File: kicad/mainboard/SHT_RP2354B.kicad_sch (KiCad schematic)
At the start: 61 parts, among them J3 USB_B_Micro, J7 Conn_01x03_Shielded, J8 Conn_01x04_Shielded, Q1 AO3401A, SW2 SW_Push_RUN, SW4 SW_Push_BOOT, U2 MCP73831-2-OT, U3 RP2350_80QFN, U5 TPS63031DSK, U6 MAINSW_CUS-12TB, U7 TFTSW_CUS-12TB, Y1 X322512MSB4SI

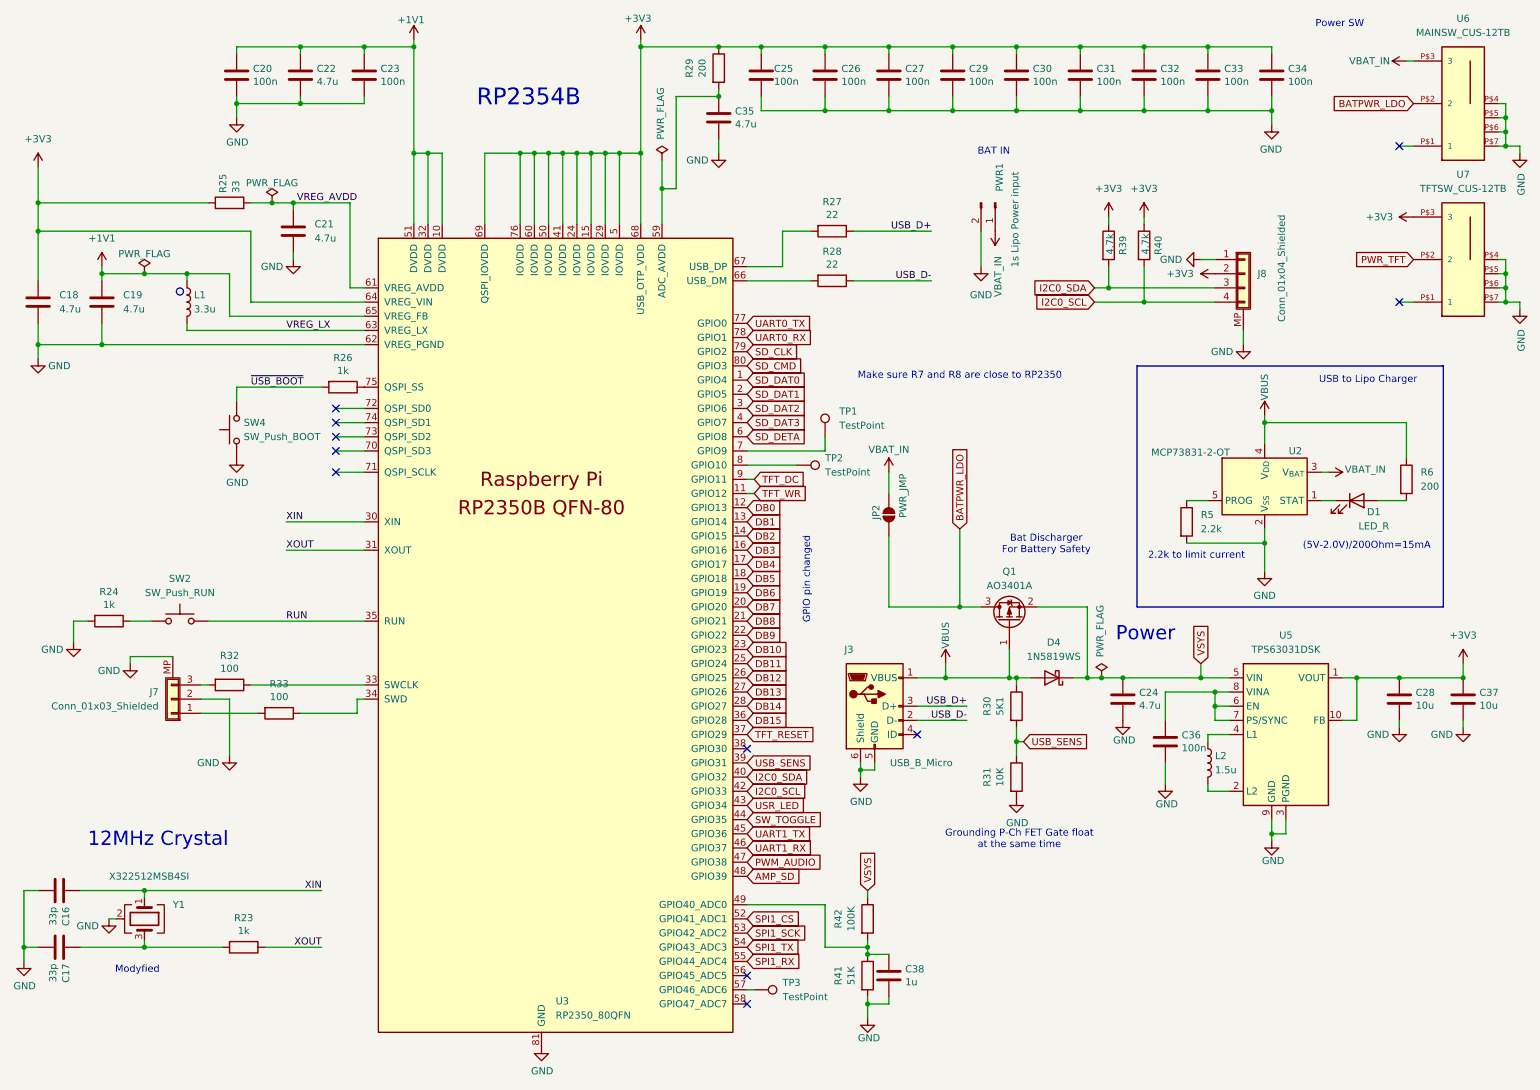
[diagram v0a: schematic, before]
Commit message: 0.960 ソフトウェア＋ドキュメント KiCad v7 基板
普段編集しないモジュールを src/ へ移動し、README を v7 に更新

■ src/ への移動（Arduino IDE のタブ削減）
Arduino IDE はスケッチ直下のファイルを全部タブに出すため 28 個まで増え、
目的のファイルを探しづらくなっていた。仕様が固まっていて普段いじらない
4 モジュールを src/ へ移し、タブを 20 個に減らした。

  src/button.*     ボタン入力・メニュー
  src/sound.*      音声出力（WAV・トーン）
  src/vectormap.*  ベクタ地図の描画
  src/imulog.*     生 IMU ロガー

src/ 配下もコンパイルされるが IDE のタブには出ない。裏を返すと IDE からは
編集できなくなるので、これらは VSCode 等で編集すること。
またスケッチ直下は include パスに入っていないため、src/ の中からルート側の
ヘッダを参照するときは "../mysd.h" のように 1 段戻る必要がある。
この経緯と注意点は GPS_TFT_map.ino のヘッダに残した。

#include は 27 箇所を書き換え、全 104 件が実在するパスへ解決することを確認。

■ 併せて修正
button.cpp の #include "Button.h" が大文字始まりだった。macOS は
ファイルシステムが大文字小文字を区別しないため通っていたが、Linux では
壊れる。"button.h" に修正。

■ README を v7 に更新
 * タイトルとスペックを v7 へ。ソフトウェアバージョン 0.942 → 0.960
 * PONS Link（機体⇄ボート テレメトリ無線）の節を新設。3 台構成、下り一方向に
   した理由、無線パラメータ、実測 350m。設計の詳細は docs/pons_link.md へ
 * BNO085 を β 試験版から標準搭載へ。SPI 接続にした理由も記載
 * マイコンを RP2350B（外付け FLASH 16MB）と明記
 * PCBA とは別に発注する部品の一覧表（Digikey / マルツ / 秋月）を追加
 * 警告音・SD ログ・使用部品に無線関連を追記

重量とバッテリー持続時間は v7 実機での計測待ちのため、v6 β版の参考値と
PONS Link の消費電流だけを記載した。水面での到達距離も未確認と明記。

普段編集しないモジュールを src/ へ移動し、README を v7 に更新

■ src/ への移動（Arduino IDE のタブ削減）
Arduino IDE はスケッチ直下のファイルを全部タブに出すため 28 個まで増え、
目的のファイルを探しづらくなっていた。仕様が固まっていて普段いじらない
4 モジュールを src/ へ移し、タブを 20 個に減らした。

  src/button.*     ボタン入力・メニュー
  src/sound.*      音声出力（WAV・トーン）
  src/vectormap.*  ベクタ地図の描画
  src/imulog.*     生 IMU ロガー

src/ 配下もコンパイルされるが IDE のタブには出ない。裏を返すと IDE からは
編集できなくなるので、これらは VSCode 等で編集すること。
またスケッチ直下は include パスに入っていないため、src/ の中からルート側の
ヘッダを参照するときは "../mysd.h" のように 1 段戻る必要がある。
この経緯と注意点は GPS_TFT_map.ino のヘッダに残した。

#include は 27 箇所を書き換え、全 104 件が実在するパスへ解決することを確認。

■ 併せて修正
button.cpp の #include "Button.h" が大文字始まりだった。macOS は
ファイルシステムが大文字小文字を区別しないため通っていたが、Linux では
壊れる。"button.h" に修正。

■ README を v7 に更新
 * タイトルとスペックを v7 へ。ソフトウェアバージョン 0.942 → 0.960
 * PONS Link（機体⇄ボート テレメトリ無線）の節を新設。3 台構成、下り一方向に
   した理由、無線パラメータ、実測 350m。設計の詳細は docs/pons_link.md へ
 * BNO085 を β 試験版から標準搭載へ。SPI 接続にした理由も記載
 * マイコンを RP2350B（外付け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
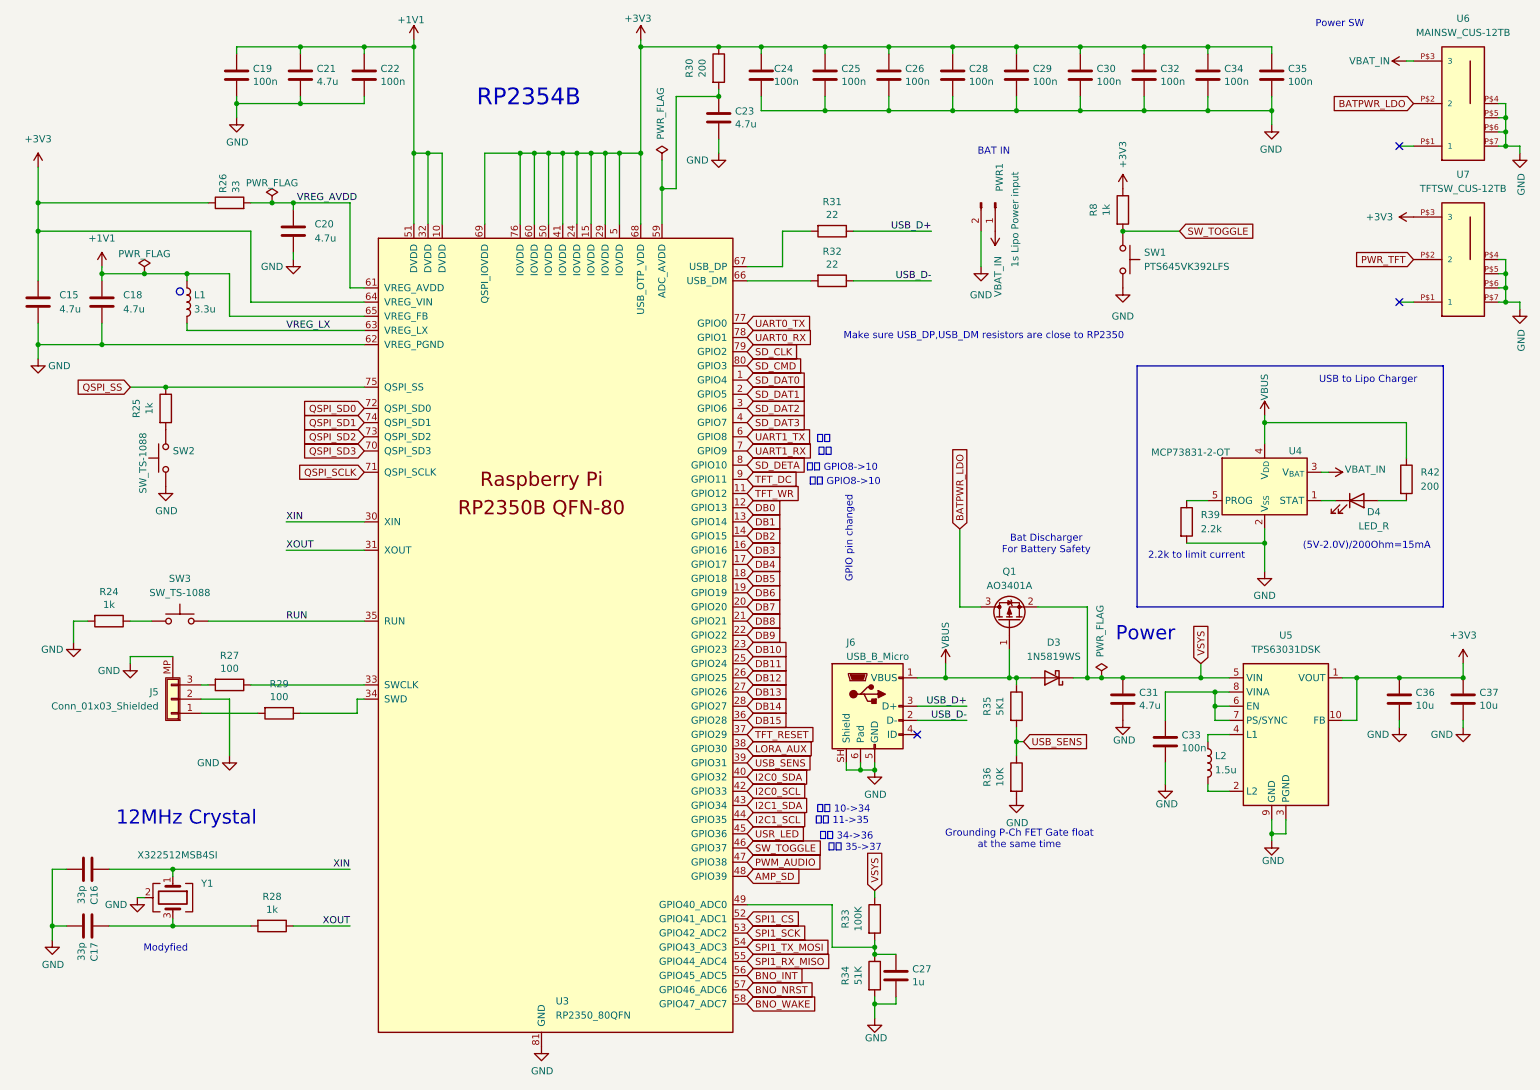
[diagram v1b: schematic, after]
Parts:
- removed J8: Conn_01x04_Shielded, Connector_JST:JST_SH_SM04B-SRSS-TB_1x04-1MP_P1.00mm_Horizontal, symbol Connector_Generic_Shielded:Conn_01x04_Shielded
- removed JP2: PWR_JMP, Jumper:SolderJumper-2_P1.3mm_Open_RoundedPad1.0x1.5mm, symbol Jumper:SolderJumper_2_Open
- removed R39, R40: 4.7k, Resistor_SMD:R_0402_1005Metric, symbol Device:R
- removed TP1, TP2, TP3: TestPoint, TestPoint:TestPoint_THTPad_D1.5mm_Drill0.7mm, symbol Connector:TestPoint
- added R8: 1k, Resistor_SMD:R_0402_1005Metric, symbol Device:R
- added SW1: PTS645VK392LFS, Button_Switch_THT:SW_Tactile_SPST_Angled_PTS645Vx39-2LFS, symbol Switch:SW_Push
- PWR1: LCSC C5251182 -> C173752; now in the parts list
- SW2: renamed from SW4; value SW_Push_BOOT -> SW_TS-1088; footprint Button_Switch_SMD:SW_Push_1P1T_NO_Vertical_Wuerth_434133025816 -> GPS_TFT:TS-1088-AR02016; LCSC C5504987 -> C720477; now in the parts list
- SW3: renamed from SW2; value SW_Push_RUN -> SW_TS-1088; footprint Button_Switch_SMD:SW_Push_1P1T_NO_Vertical_Wuerth_434133025816 -> GPS_TFT:TS-1088-AR02016; LCSC C5504987 -> C720477; now in the parts list
- U3: LCSC C39843328 -> C42415655
- U6, U7: footprint GPS_TFT:CUS-12B -> GPS_TFT:CUS-12TB
- renumbered C18 to C15, C19 to C18, C20 to C19, C21 to C20, C22 to C21, C23 to C22, C35 to C23, C25 to C24, C26 to C25, C27 to C26, C38 to C27, C29 to C28, C30 to C29, C31 to C30, C24 to C31, C36 to C33, C33 to C34, C34 to C35, C28 to C36, D4 to D3, D1 to D4, J7 to J5, J3 to J6, R26 to R25, R25 to R26, R32 to R27, R23 to R28, R33 to R29, R29 to R30, R27 to R31, R28 to R32, R42 to R33, R41 to R34, R30 to R35, R31 to R36, R5 to R39, R6 to R42, U2 to U4
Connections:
- net +3V3: now also R8.1
- net GND: now also J6.SH (Shield), SW1.2
- net SD_DETA: now also U3.8 (GPIO10); no longer U3.6 (GPIO8)
- net SW_TOGGLE: now also U3.46 (GPIO37), R8.2, SW1.1; no longer U3.44 (GPIO35)
- net UART1_RX: now also U3.7 (GPIO9); no longer U3.46 (GPIO37)
- net UART1_TX: now also U3.6 (GPIO8); no longer U3.45 (GPIO36)
- net USR_LED: now also U3.45 (GPIO36); no longer U3.43 (GPIO34)
- net BNO_NRST: now reaches U3.57 (GPIO46_ADC6)
- net LORA_AUX: now reaches U3.38 (GPIO30)
- net BNO_INT: now reaches U3.56 (GPIO45_ADC5)
- net BNO_WAKE: now reaches U3.58 (GPIO47_ADC7)
- net QSPI_SD3: now reaches U3.70 (QSPI_SD3)
- net QSPI_SCLK: now reaches U3.71 (QSPI_SCLK)
- net QSPI_SD0: now reaches U3.72 (QSPI_SD0)
- net QSPI_SD2: now reaches U3.73 (QSPI_SD2)
- net QSPI_SD1: now reaches U3.74 (QSPI_SD1)
- net QSPI_SS: now reaches R25.1, U3.75 (QSPI_SS)
- net SPI1_RX renamed SPI1_RX_MISO
- net SPI1_TX renamed SPI1_TX_MOSI
- net ~{USB_BOOT}: no longer names the net of R25.2, SW2.2
- new net I2C1_SCL: U3.44 (GPIO35)
- new net I2C1_SDA: U3.43 (GPIO34)
- no-connect marks 11 -> 3
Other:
- note added: "Make sure USB_DP,USB_DM resistors are close to RP2350"
- note added: "移動"
- note added: "移動 10->34"
- note added: "移動 11->35"
- note added: "移動 34->36"
- note added: "移動 35->37"
- note added: "移動 GPIO8->10"
- note removed: "Make sure R7 and R8 are close to RP2350"
- title: PONS for HPA v6 -> PONS for HPA v7
- moved on the sheet: C16, C17, C27, R25, R28, R33, R34, SW2, Y1

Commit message: kicadデータ更新
KiCad プロジェクトを自己完結化（ライブラリテーブルと独自シンボルの取り込み）

クローンしただけでは GPS_TFT: などのライブラリが解決できず、また一部の
シンボルが KiCad 標準ライブラリ本体を書き換えて作られていたため、他の環境
では正しく再現できない状態だった。プロジェクト内で完結するよう整理した。

■ ライブラリテーブルを追加
fp-lib-table / sym-lib-table がリポジトリに一度も入っていなかった。
3 プロジェクト分を ${KIPRJMOD} 相対で新規作成。絶対パスを使っていないので
どこへ置いても、どのマシンでも解決する。
回路図が別名で参照している nickname（2005280040 / 54132-4062 / CUS-12TB /
RP2350_80QFN_minimal）も同じフォルダを指すよう登録した。

■ 標準ライブラリへの依存を解消
6 つの標準ライブラリがローカルで書き換えられていた（codesign --verify で
確認）。使用中のシンボルを上流 kicad-symbols 10.0.6 と 1 つずつ比較し、
差があるものだけプロジェクト内へ移した。

  追加されていたもの
    RF_Module:E220-900T22S(JP)  → E220-900T22S:E220-900T22S(JP)
    Sensor_Motion:BNO085        → bno085:BNO085
    Switch:CUS-12TB             → CUS-12TB:CUS-12TB

  公式シンボルを改変していたもの（ピン番号が変わるため影響が大きい）
    Connector:USB_B_Micro       → USB_microB:USB_B_Micro
      上流は 1-5,SH。手元はシールドパッドのピン 6 を追加した版
    Connector_Generic_Shielded:Conn_01x03_Shielded
                                → Conn_01x03_Shielded:Conn_01x03_Shielded
      上流はシールドピンが SH。手元は MP に改名した版

  上流と一致していたもの（標準ライブラリのまま参照する）
    Conn_01x02_Pin / Conn_01x04_Pin / Micro_SD_Card_Det2 /
    TestPoint_2Pole / SW_Push

改変版と上流の差は sym-lib-table の descr に書いてある。

■ 整理
 * DMG3415U.kicad_sym は中身が DMP2045 だったので dmp2045.kicad_sym へ改名
   （回路図の参照 dmp2045:DMP2045 が切れていたのを修復）
 * 未使用のフットプリント 6 件とシンボル 5 件を削除
 * .gitignore のパターンがプロジェクト名を直書きしていて v7 のバックアップ
   フォルダに当たっていなかったため、*-backups/ 等の総称に変更

回路図の lib_id を貼り替えただけで、シンボル本体・ピン・フットプリント指定は
変えていない。ネットリストと部品構成に変更はなく、発注済みの基板データにも
影響しない。全 158 件の参照が解決することを確認済み。
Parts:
- J5: symbol Connector_Generic_Shielded:Conn_01x03_Shielded -> Conn_01x03_Shielded:Conn_01x03_Shielded
- J6: symbol Connector:USB_B_Micro -> USB_microB:USB_B_Micro
- U6, U7: symbol Switch:CUS-12TB -> CUS-12TB:CUS-12TB
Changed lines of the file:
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@@
 	)
 	(symbol
-		(lib_id "Connector_Generic_Shielded:Conn_01x03_Shielded")
+		(lib_id "Conn_01x03_Shielded:Conn_01x03_Shielded")
 		(at 40.64 135.89 180)
 		(unit 1)
@@
 	(symbol
 		(lib_name "CUS-12TB_1")
-		(lib_id "Switch:CUS-12TB")
+		(lib_id "CUS-12TB:CUS-12TB")
 		(at 270.51 29.21 0)
 		(unit 1)
@@
 	)
 	(symbol
-		(lib_id "Connector:USB_B_Micro")
+		(lib_id "USB_microB:USB_B_Micro")
 		(at 166.37 137.16 0)
 		(unit 1)
@@
 	)
 	(symbol
-		(lib_id "Switch:CUS-12TB")
+		(lib_id "CUS-12TB:CUS-12TB")
 		(at 270.51 57.15 0)
 		(unit 1)

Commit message: 0.961 KiCad更新 wav更新
wav雑音除去
kicad更新（スイッチ背面、DocへのQRコード更新）
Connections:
- net GND: now also SW1.1; no longer SW1.2
- net SW_TOGGLE: now also SW1.2; no longer SW1.1
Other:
- moved on the sheet: SW1
